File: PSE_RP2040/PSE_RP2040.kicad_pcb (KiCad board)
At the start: 2 copper layers, 100 x 60 mm, 128 parts, among them IC1 LAN8742A-CZ, IC2 SAM-M8Q-0, J1 USB_B, J2 USB_B_Mini, J3 8P8C_LED, J4 Conn_01x03, J5 Screw_Terminal_01x02, Q2 IRLML6402, SW1 SW_Push, SW2 SW_Push, T1 749013011, U1 RP2040, U2 PCF8563T, U4 USBLC6-4SC6, U5 W25Q16JVUSSQ, U6 PAM7Q, U7 TPS2375-1, U8 LMR16006YQ, Y1 Crystal_GND3, Y2 Crystal_GND24, Y3 25MHz

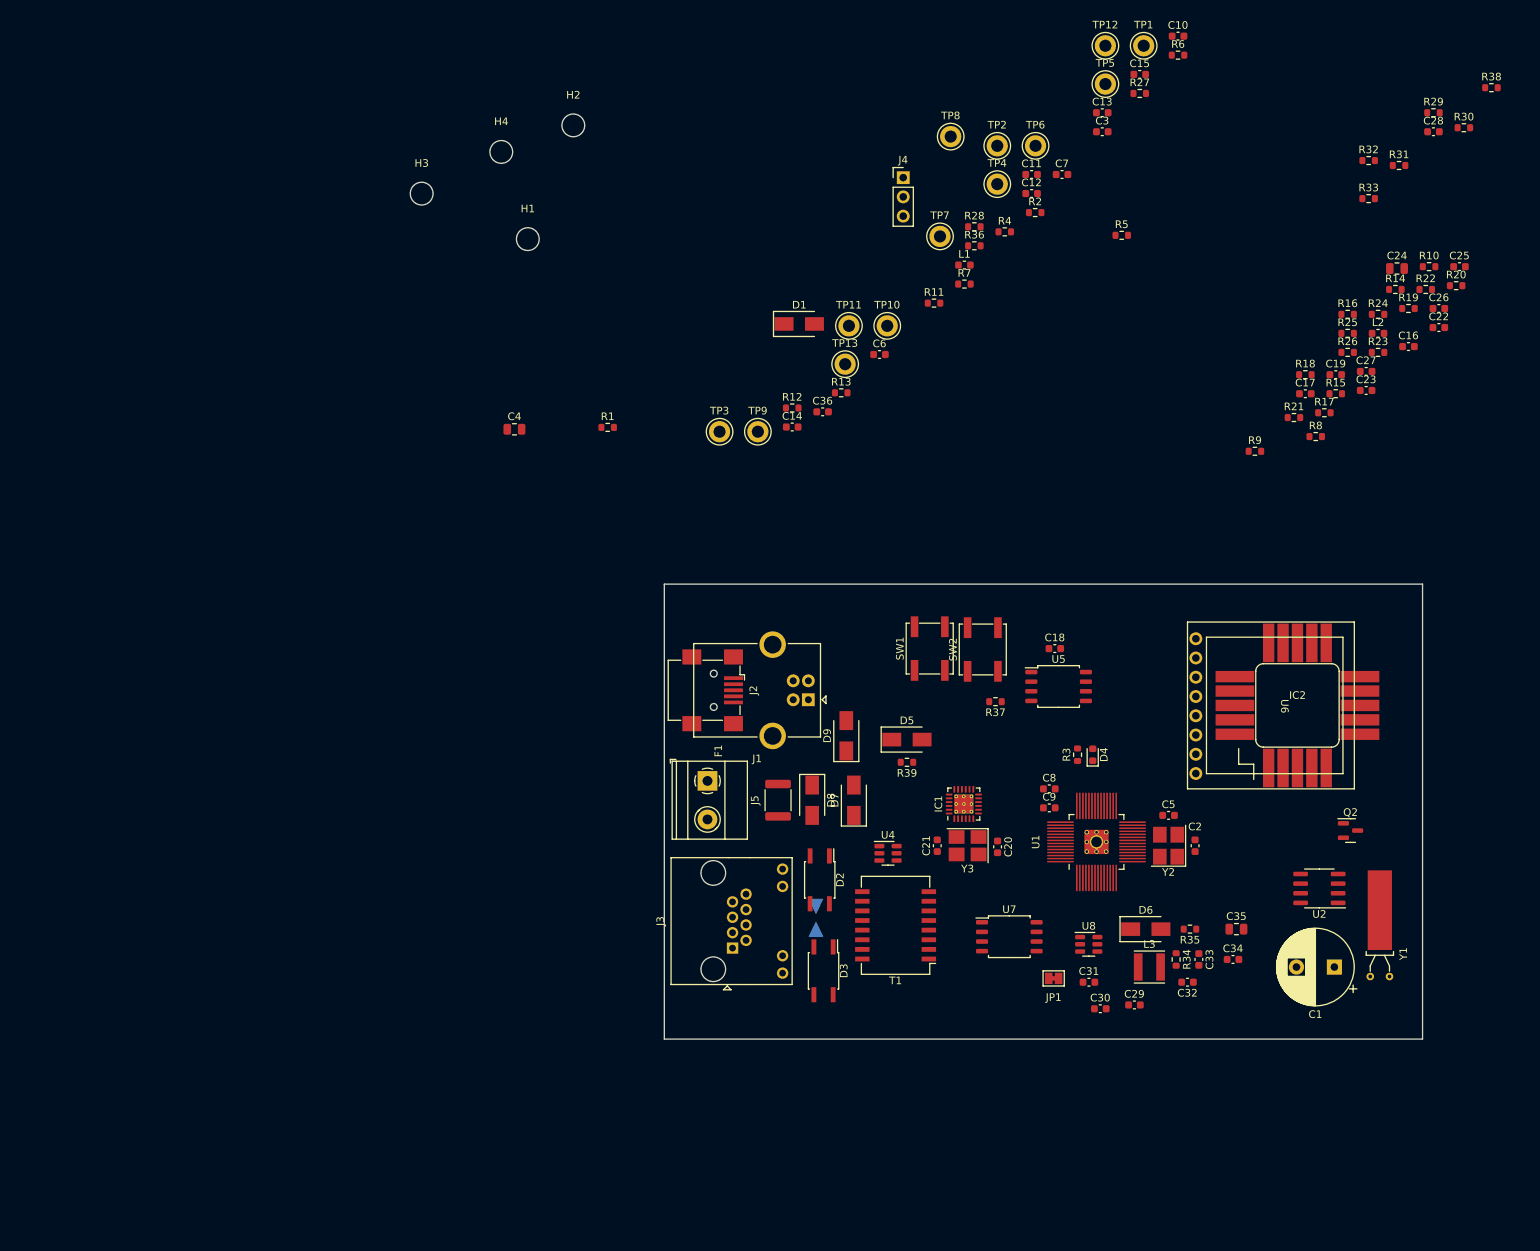
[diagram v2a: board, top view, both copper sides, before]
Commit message: piazzamento componenti pcb
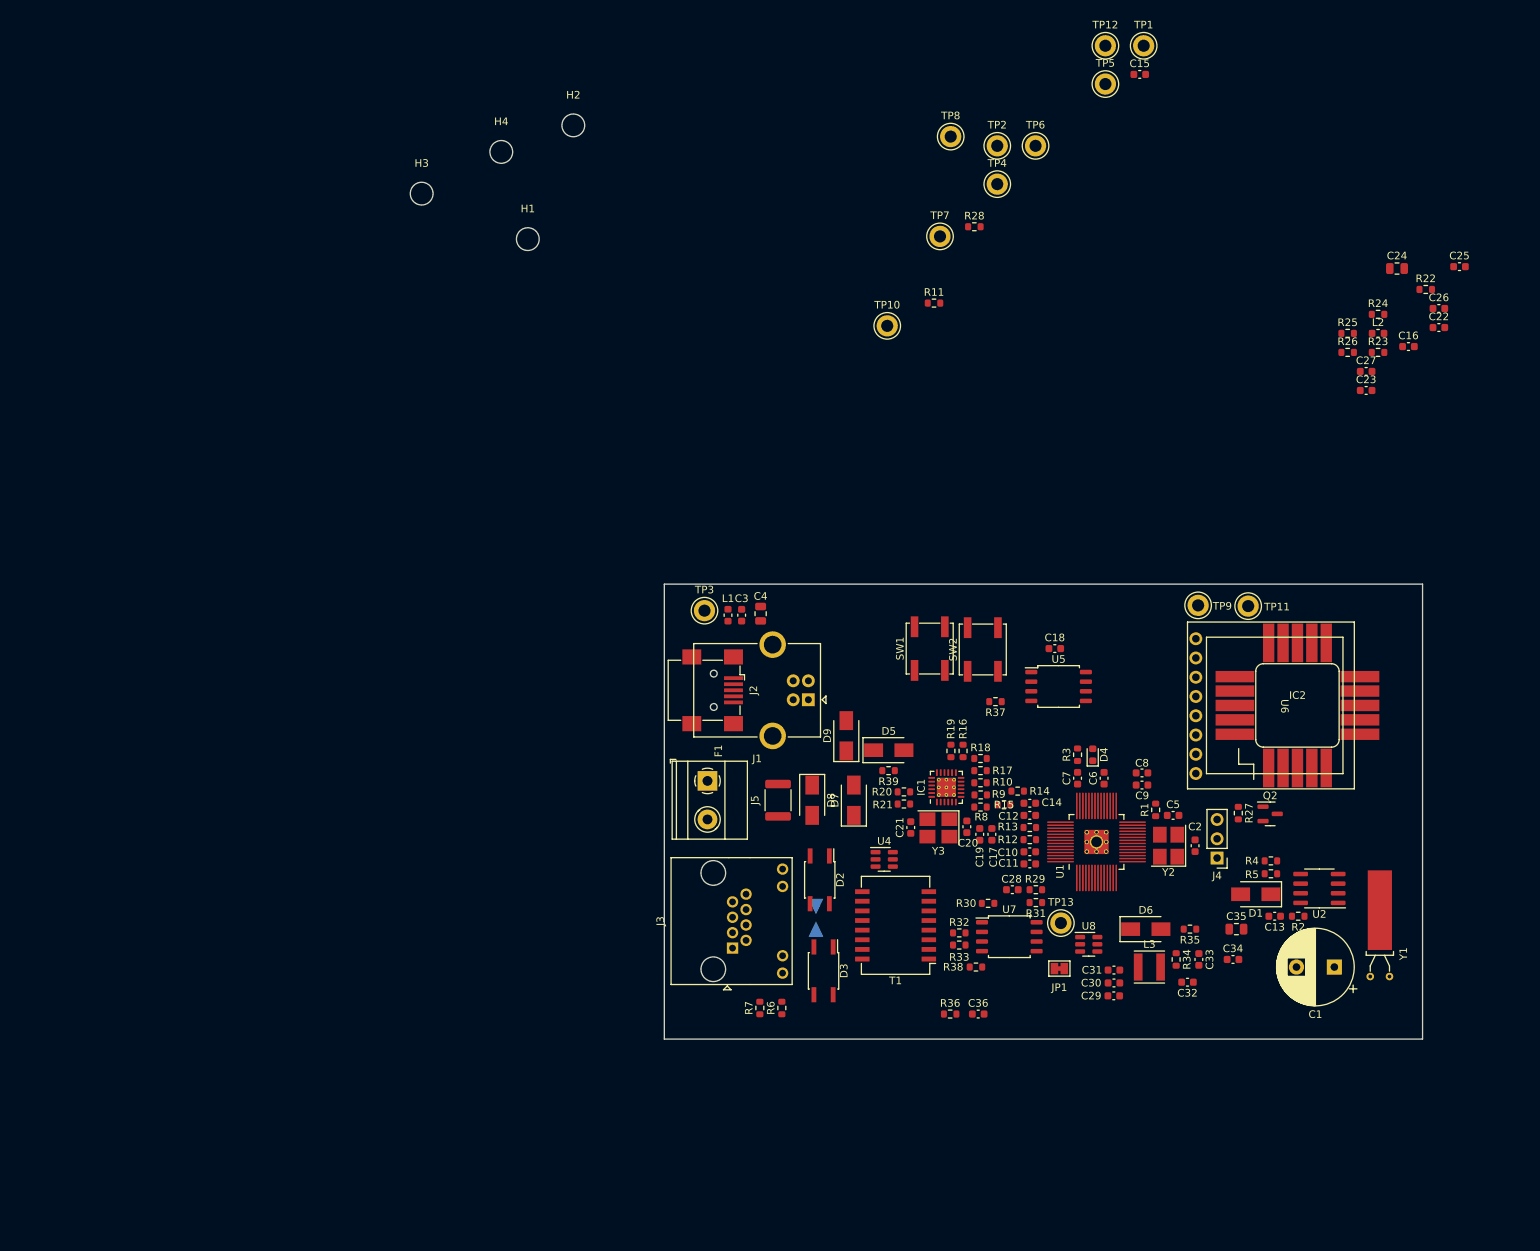
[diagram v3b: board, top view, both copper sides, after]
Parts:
- moved R6 136.1 mm to (115.5, 155.9), turned to 90 degrees
- moved R38 134.4 mm to (141.1, 150.5), turned to 180 degrees
- moved R30 120.0 mm to (142.7, 142.1)
- moved R32 115.3 mm to (138.9, 146.0), turned to 180 degrees
- moved R29 115.1 mm to (149.0, 140.3), turned to 180 degrees
- moved C28 114.4 mm to (145.9, 140.3), turned to 180 degrees
- moved R33 112.3 mm to (138.9, 147.6)
- moved C10 109.3 mm to (148.2, 135.3), turned to 180 degrees
- moved C13 108.4 mm to (180.5, 143.8), turned to 180 degrees
- moved R31 108.4 mm to (149.0, 142.0), turned to 180 degrees
- moved R36 101.4 mm to (137.7, 156.7)
- moved R7 99.2 mm to (112.6, 155.9), turned to 90 degrees
- moved R2 99.1 mm to (183.6, 143.8), turned to 180 degrees
- moved J4 98.8 mm to (172.9, 136.1), turned to 180 degrees
- moved R20 98.8 mm to (131.6, 127.4), turned to 180 degrees
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
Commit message: contorni raspberry pi 4
mantenersi entro i 56 mm di larghezza. in lunghezza si può andare oltre gli 85 mm
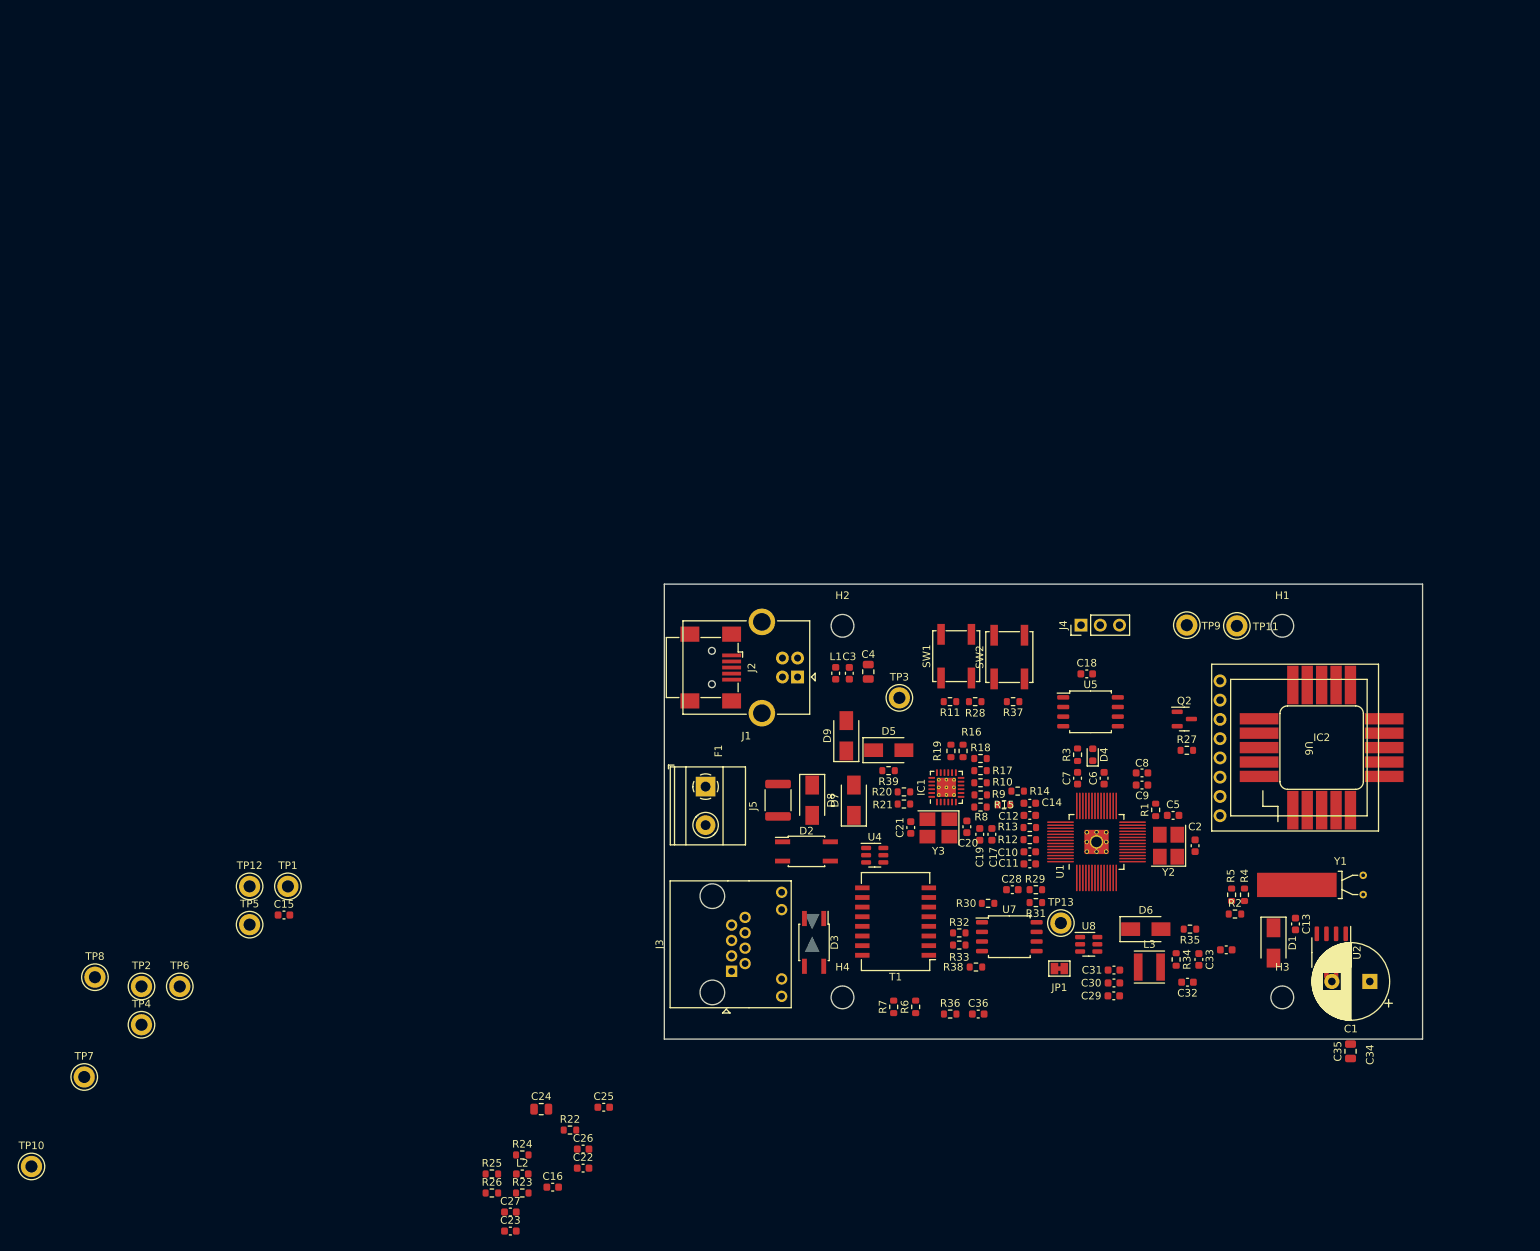
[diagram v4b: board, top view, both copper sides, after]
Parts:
- moved TP10 158.2 mm to (16.5, 176.8)
- moved TP12 158.2 mm to (45.3, 139.9)
- moved TP6 158.2 mm to (36.1, 153.1)
- moved TP7 158.2 mm to (23.5, 165.0)
- moved TP8 158.2 mm to (24.9, 151.8)
- moved C15 158.2 mm to (49.8, 143.6)
- moved C16 158.2 mm to (85.3, 179.5)
- moved C22 158.2 mm to (89.3, 177.0)
- moved C23 158.2 mm to (79.7, 185.3)
- moved C24 158.2 mm to (83.8, 169.2)
- moved C25 158.2 mm to (92.0, 169.0)
- moved C26 158.2 mm to (89.3, 174.5)
- moved C27 158.2 mm to (79.7, 182.8)
- moved L2 158.2 mm to (81.3, 177.8)
- moved R22 158.2 mm to (87.6, 172.0)
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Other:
- board text added: "footprint Rpi4"

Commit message: pad micro, footprint, posizionamento componenti pcb
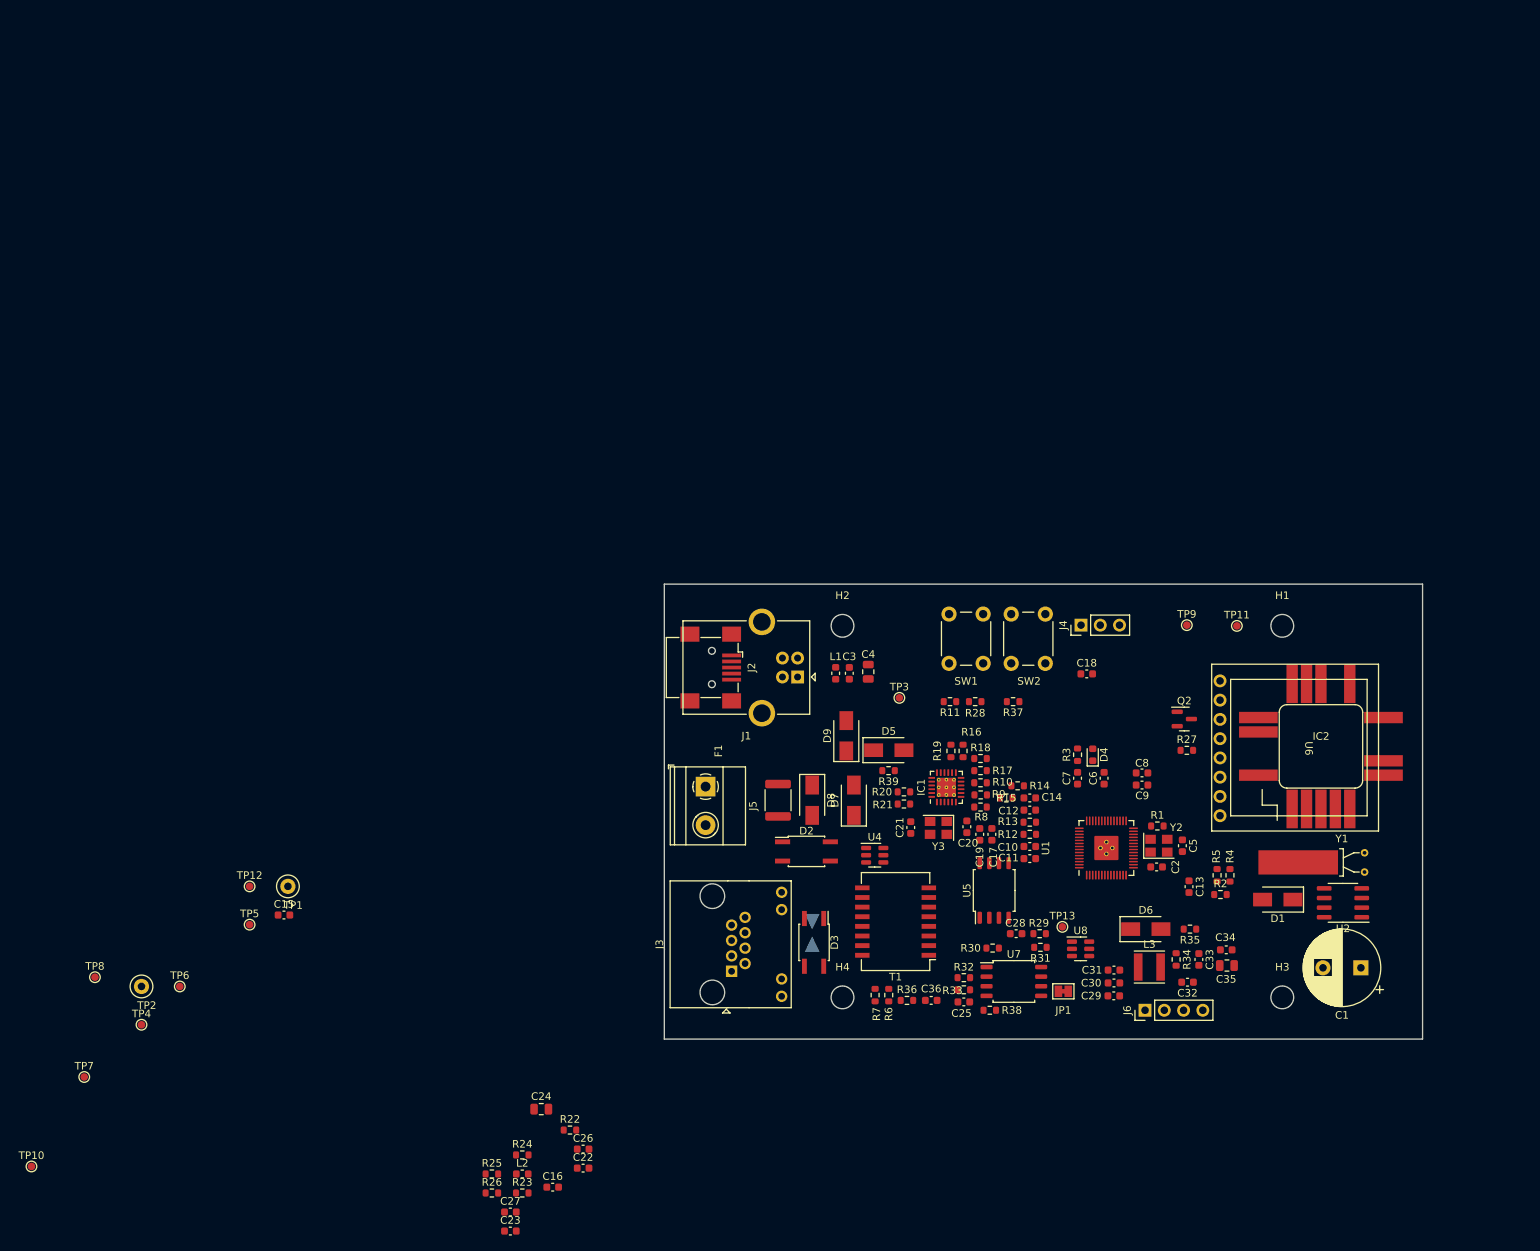
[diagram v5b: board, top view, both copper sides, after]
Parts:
- added J6: Conn_01x04_Female, Connector_PinHeader_2.54mm:PinHeader_1x04_P2.54mm_Vertical, F.Cu at (163.4, 156.2)
- SW1, SW2: footprint Button_Switch_SMD:SW_SPST_EVQP0 -> Button_Switch_THT:SW_PUSH_6mm
- TP1, TP2: footprint TestPoint:TestPoint_Keystone_5005-5009_Compact -> TestPoint:TestPoint_Loop_D1.80mm_Drill1.0mm_Beaded
- TP10, TP11, TP12, TP13, TP3, TP4, TP5, TP6, TP7, TP8, TP9: footprint TestPoint:TestPoint_Keystone_5005-5009_Compact -> TestPoint:TestPoint_Pad_D1.0mm
- Y2, Y3: footprint Crystal:Crystal_SMD_3225-4Pin_3.2x2.5mm_HandSoldering -> Crystal:Crystal_SMD_3225-4Pin_3.2x2.5mm
- moved C25 49.5 mm to (139.5, 155.1)
- moved U5 26.8 mm to (143.5, 140.4), turned to 90 degrees
- moved C35 19.8 mm to (174.2, 150.3), turned to 0 degrees
- moved C13 14.9 mm to (169.2, 139.9)
- moved U2 6.74 mm to (189.5, 142.0), turned to 180 degrees
- moved C36 6.46 mm to (135.2, 154.9)
- moved R38 5.99 mm to (142.9, 156.2), turned to 0 degrees
- moved R36 5.98 mm to (132.0, 154.9)
- moved R30 5.93 mm to (143.3, 148.0)
- moved R31 5.93 mm to (149.6, 147.9)
- moved R32 5.93 mm to (139.5, 151.9)
- moved R33 5.93 mm to (139.5, 153.5)
- moved U7 5.93 mm to (146.1, 152.4)
- moved C28 5.82 mm to (146.4, 146.1)
- moved R29 5.82 mm to (149.5, 146.1)
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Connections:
- net /GPIO25 renamed /GPIO_LED
- U1 pad 29: /GPIO18 -> unconnected-(U1-Pad29)
- U1 pad 30: /GPIO19 -> unconnected-(U1-Pad30)
- U1 pad 32: /GPIO21 -> unconnected-(U1-Pad32)
- U1 pad 34: /GPIO22_R -> unconnected-(U1-Pad34)
- U1 pad 35: /GPIO23_G -> unconnected-(U1-Pad35)
- U1 pad 36: /GPIO24_B -> unconnected-(U1-Pad36)
